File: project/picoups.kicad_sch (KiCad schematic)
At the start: 20 parts, among them J1 VIN, J2 BATT, J3 USB_C_Receptacle, J4 Conn_02x20_Odd_Even, Q1 Q_PMOS_GSD, SW2 SW_USER, U6 M41T62

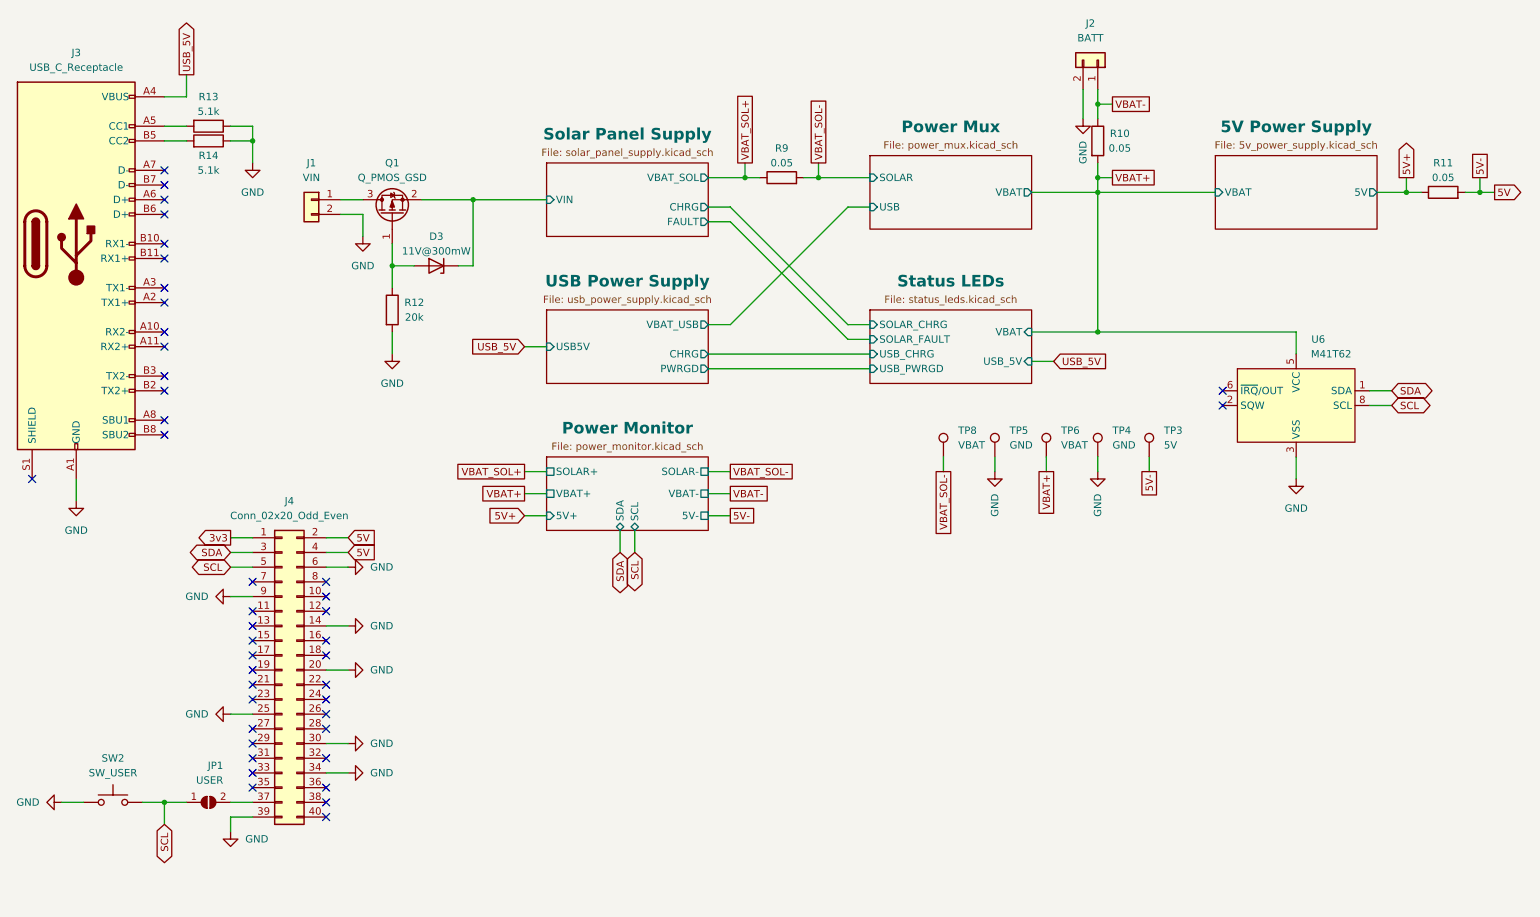
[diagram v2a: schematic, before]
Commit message: Fixed solar status LEDs wrong VBAT
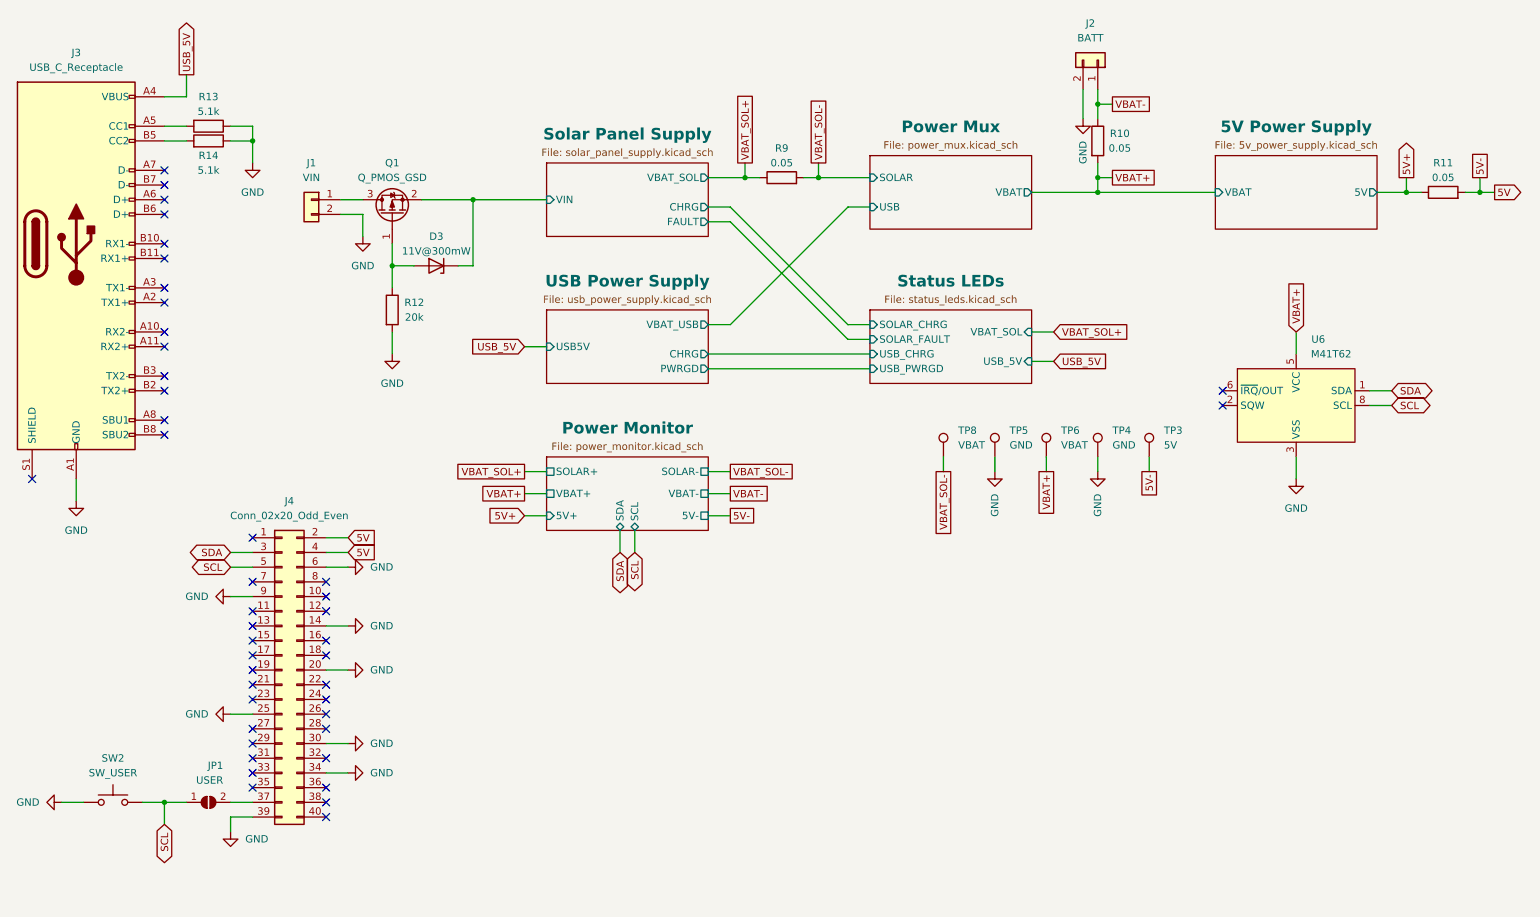
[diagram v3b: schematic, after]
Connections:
- net 3v3: no longer names the net of J4.1 (Pin_1)
- no-connect marks 43 -> 44
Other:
- sheet Status LEDs ports: added VBAT_SOL; removed VBAT
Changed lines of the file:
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@@
   (junction (at 207.01 31.75) (diameter 0) (color 0 0 0 0)
-  )
-  (junction (at 207.01 71.12) (diameter 0) (color 0 0 0 0)
   )
   (junction (at 158.75 44.45) (diameter 0) (color 0 0 0 0)
@@
   (no_connect (at 73.66 137.16))
   (no_connect (at 45.72 45.72))
+  (no_connect (at 60.96 106.68))
   (no_connect (at 60.96 139.7))
   (no_connect (at 73.66 116.84))
@@
     (stroke (width 0) (type default))
   )
-  (wire (pts (xy 241.3 71.12) (xy 207.01 71.12))
-    (stroke (width 0) (type default))
-  )
   (wire (pts (xy 45.72 152.4) (xy 49.53 152.4))
     (stroke (width 0) (type default))
@@
     (stroke (width 0) (type default))
   )
-  (wire (pts (xy 207.01 46.99) (xy 207.01 71.12))
-    (stroke (width 0) (type default))
-  )
   (wire (pts (xy 96.52 59.69) (xy 99.06 59.69))
     (stroke (width 0) (type default))
@@
     (stroke (width 0) (type default))
   )
-  (wire (pts (xy 195.58 71.12) (xy 207.01 71.12))
-    (stroke (width 0) (type default))
-  )
   (wire (pts (xy 139.7 99.06) (xy 143.51 99.06))
     (stroke (width 0) (type default))
@@
     (stroke (width 0) (type default))
   )
-  (wire (pts (xy 57.15 106.68) (xy 60.96 106.68))
-    (stroke (width 0) (type default))
-  )
   (wire (pts (xy 57.15 109.22) (xy 60.96 109.22))
     (stroke (width 0) (type default))
@@
   )
   (wire (pts (xy 139.7 44.45) (xy 146.05 44.45))
+    (stroke (width 0) (type default))
+  )
+  (wire (pts (xy 195.58 71.12) (xy 199.39 71.12))
     (stroke (width 0) (type default))
   )
@@
     )
   )
-  (global_label "3v3" (shape output) (at 57.15 106.68 180) (fields_autoplaced)
-    (effects (font (size 1.27 1.27)) (justify right))
-    (property "Intersheetrefs" "${INTERSHEET_REFS}" (at 50.8576 106.68 0)
-      (effects (font (size 1.27 1.27)) (justify right) hide)
-    )
-  )
   (global_label "5V+" (shape input) (at 107.95 102.87 180) (fields_autoplaced)
     (effects (font (size 1.27 1.27)) (justify right))
@@
   (global_label "VBAT_SOL+" (shape passive) (at 146.05 41.91 90) (fields_autoplaced)
     (effects (font (size 1.27 1.27)) (justify left))
-    (property "Intersheetrefs" "${INTERSHEET_REFS}" (at 146.05 29.5926 90)
+    (property "Intersheetrefs" "${INTERSHEET_REFS}" (at 146.05 29.5132 90)
       (effects (font (size 1.27 1.27)) (justify left) hide)
     )
@@
     )
   )
+  (global_label "VBAT_SOL+" (shape input) (at 199.39 71.12 0) (fields_autoplaced)
+    (effects (font (size 1.27 1.27)) (justify left))
+    (property "Intersheetrefs" "${INTERSHEET_REFS}" (at 212.8981 71.12 0)
+      (effects (font (size 1.27 1.27)) (justify left) hide)
+    )
+  )
   (global_label "USB_5V" (shape input) (at 199.39 76.2 0) (fields_autoplaced)
     (effects (font (size 1.27 1.27)) (justify left))
@@
     (effects (font (size 1.27 1.27)) (justify left))
     (property "Intersheetrefs" "${INTERSHEET_REFS}" (at 155.8274 95.25 0)
+      (effects (font (size 1.27 1.27)) (justify left) hide)
+    )
+  )
+  (global_label "VBAT+" (shape input) (at 241.3 71.12 90) (fields_autoplaced)
+    (effects (font (size 1.27 1.27)) (justify left))
+    (property "Intersheetrefs" "${INTERSHEET_REFS}" (at 241.3 62.1476 90)
       (effects (font (size 1.27 1.27)) (justify left) hide)
     )
@@
       (effects (font (size 1.27 1.27)) (justify top))
     )
-    (pin "VBAT" input (at 195.58 71.12 0)
-      (effects (font (size 1.27 1.27)) (justify right))
-    )
     (pin "SOLAR_CHRG" input (at 167.64 69.85 180)
       (effects (font (size 1.27 1.27)) (justify left))
@@
       (effects (font (size 1.27 1.27)) (justify right))
     )
+    (pin "VBAT_SOL" input (at 195.58 71.12 0)
+      (effects (font (size 1.27 1.27)) (justify right))
+    )

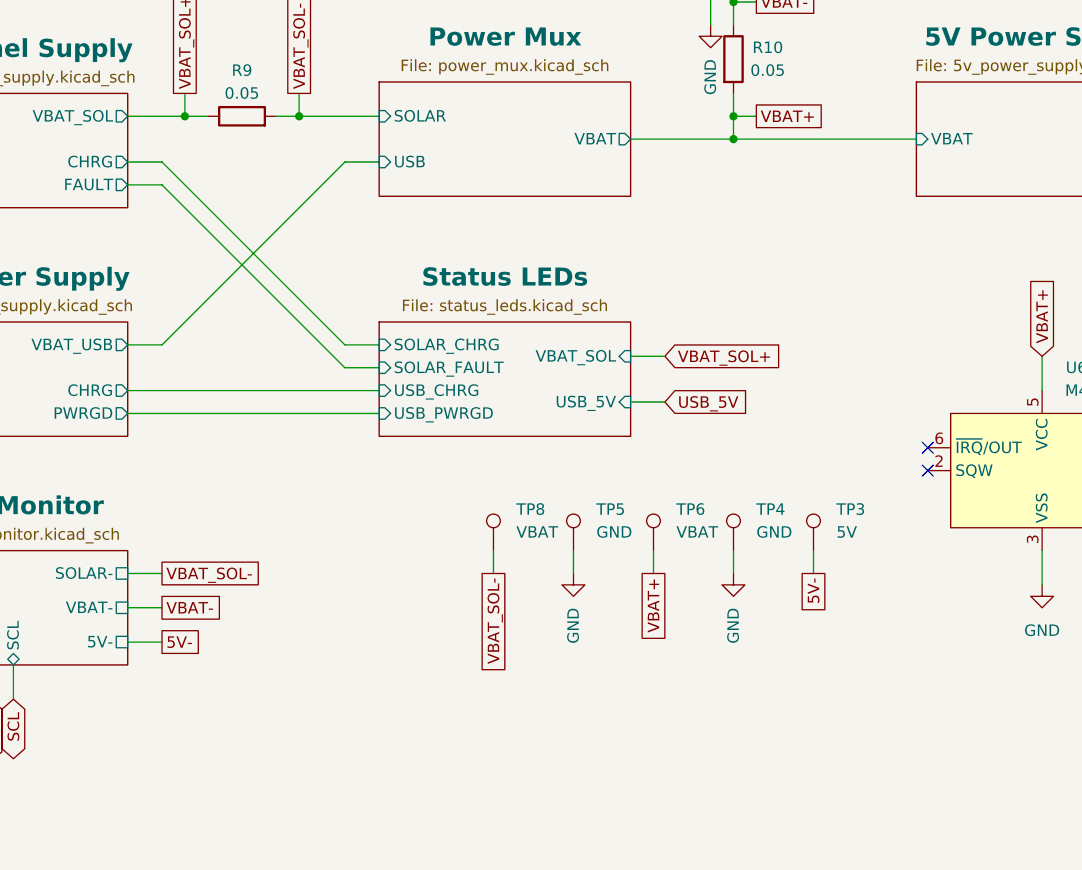
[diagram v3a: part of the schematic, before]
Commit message: Moved 5V supply
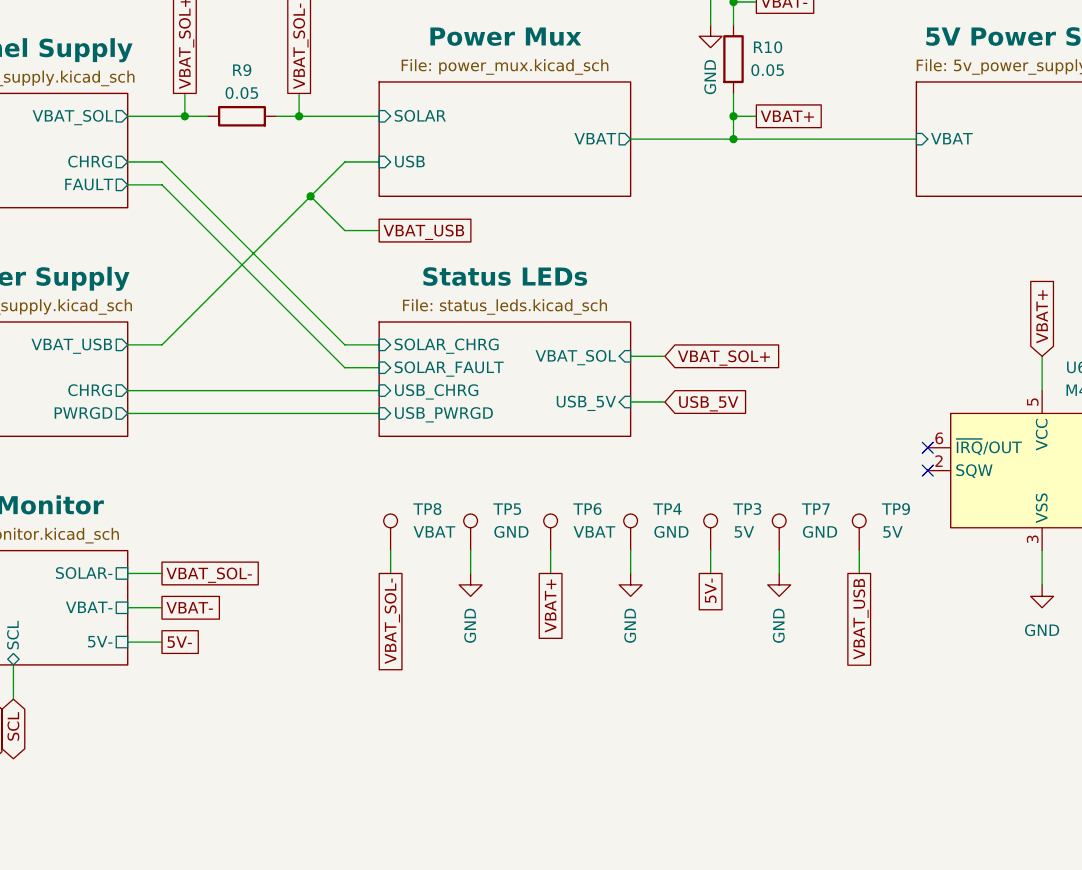
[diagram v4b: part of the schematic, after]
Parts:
- added TP7: GND, TestPoint:TestPoint_Pad_D1.0mm, symbol Connector:TestPoint
- added TP9: 5V, TestPoint:TestPoint_Pad_D1.0mm, symbol Connector:TestPoint
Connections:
- net GND: now also TP7.1
- new net VBAT_USB: TP9.1
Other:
- moved on the sheet: TP3, TP4, TP5, TP6, TP8
